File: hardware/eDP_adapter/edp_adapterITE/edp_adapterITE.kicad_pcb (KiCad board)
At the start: 4 copper layers, 36.3 x 28.4 mm, 78 parts, among them J1 DF12NB(3.0)-30DS-0.5V(51), J2 DF12NB(3.0)-30DS-0.5V(51), J3 Conn_01x30, J4 Barrel_Jack_MountingPin, J5 Conn_01x06_Socket, U1 AMS1117-1.8, U2 TLV62569APDRL, U3 MT3608, U4 IT6251, X1 27MHz

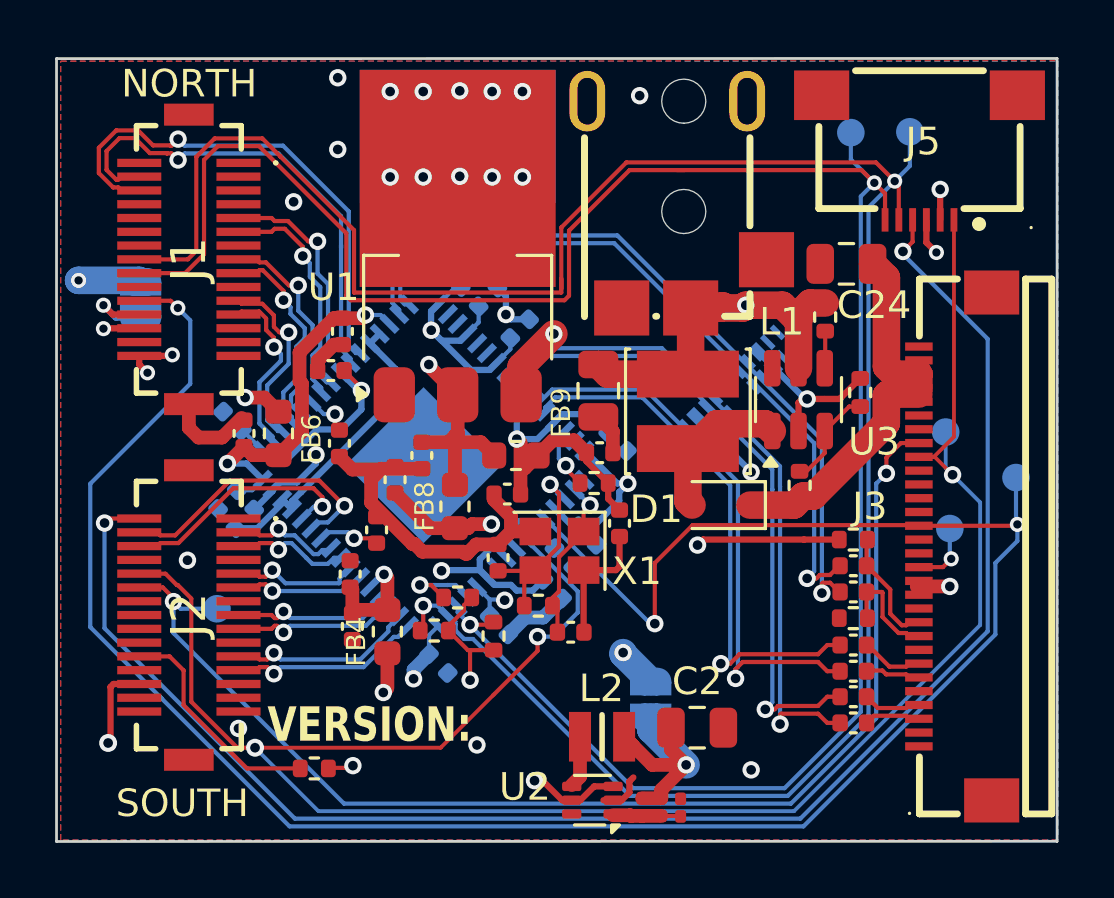
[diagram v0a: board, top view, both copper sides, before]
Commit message: add output serpentines to eDP adapter "B" board
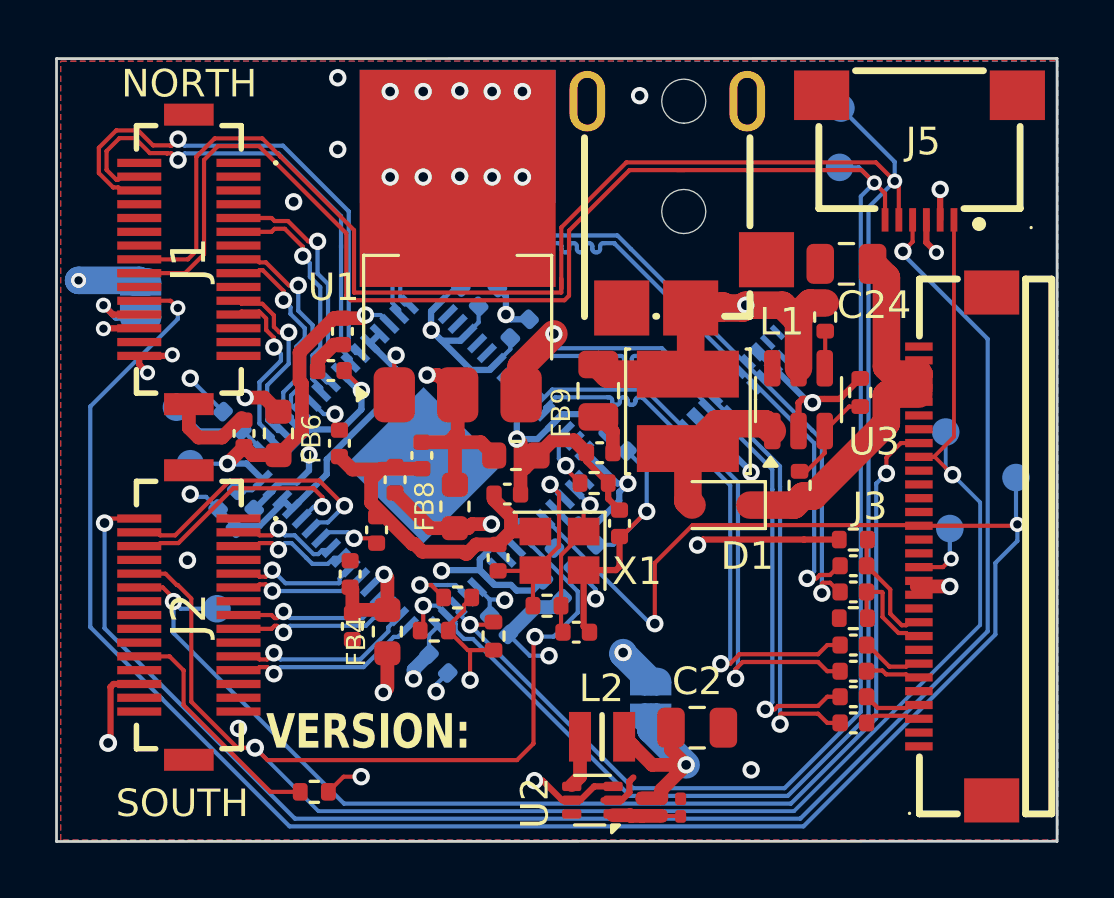
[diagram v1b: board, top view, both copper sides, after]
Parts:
- removed R18: 1M, Resistor_SMD:R_0402_1005Metric
- added R3: 1M, Resistor_SMD:R_0402_1005Metric, F.Cu at (121.4, 132.8)
- added TP2: TestPoint_Small, TestPoint:TestPoint_Pad_D1.0mm, B.Cu at (108.0, 125.5)
- added TP3: TestPoint_Small, TestPoint:TestPoint_Pad_D1.0mm, B.Cu at (108.5, 127.6)
- moved TP13 2.64 mm to (132.1, 114.7)
- moved TP14 1.33 mm to (132.0, 116.8)
- moved R9 0.85 mm to (113.0, 139.5)
- moved C19 0.20 mm to (122.5, 133.7)
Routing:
- net GND: track 57.7 -> 73.9 mm, vias 13 -> 19
- net +1V8: track 43.6 -> 46.3 mm
- net ANVDD_1V8: track 58.2 -> 60.9 mm
- net +3V3: track 107.4 -> 110.0 mm
- net PSEL: track 74.5 -> 76.8 mm
- net SDA: track 83.3 -> 84.7 mm
- net IVDD_1V8: track 30.9 -> 32.2 mm
- net /DPAUX_P: track 26.0 -> 27.3 mm
- net /DPO1_P: track 23.2 -> 24.0 mm
- net AVCC_3V3: track 49.2 -> 49.9 mm
- net SCK: track 80.6 -> 79.9 mm
- net /DPO0_P: track 19.7 -> 20.4 mm
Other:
- board text added: "eDP Adapter {dblquote}B{dblquote} v0.09"
- board text removed: "eDP Adapter IT v0.09"

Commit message: change 6-pin I2C connector to one with top contacts
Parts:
- J5: footprint easyeda2kicad:FPC-SMD_FH52K-6S-0.5SH -> easyeda2kicad:CONN-SMD_527450697; moved to B.Cu
- moved TP14 3.49 mm to (129.1, 118.8)
- moved J3 3.35 mm to (136.2, 127.2)
- moved C2 3.00 mm to (124.4, 135.5), turned to 90 degrees
- moved L2 2.46 mm to (121.5, 136.0)
- moved U2 2.46 mm to (121.1, 138.3)
- moved R11 2.46 mm to (123.6, 138.5)
- moved R12 2.46 mm to (124.3, 138.6)
- moved C6 2.46 mm to (122.9, 138.5)
- moved TP7 2.14 mm to (135.4, 127.9)
- moved J5 1.64 mm to (134.3, 118.0), turned to -90 degrees
- moved R9 1.21 mm to (113.1, 138.3)
- moved TP13 0.93 mm to (131.2, 114.9)
- moved TP5 0.79 mm to (135.4, 125.8)
- moved JP2 0.70 mm to (125.4, 135.5)
- moved R19 0.68 mm to (130.9, 127.8), turned to 180 degrees
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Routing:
- net /IO/TP_INT: track 59.2 -> 68.1 mm, vias 2 -> 1
- net GND: track 73.9 -> 82.7 mm, vias 19 -> 28
- net /IO/LCD_PWM: track 44.7 -> 49.7 mm
- net +3V3_DISP: track 24.7 -> 28.2 mm
- net TX1_N: track 2.05 -> 4.46 mm
- net SDA: track 84.7 -> 82.3 mm
- net +3V3: track 110.0 -> 107.8 mm
- net TX0_N: track 1.98 -> 4.14 mm
- net TX1_P: track 2.11 -> 4.19 mm
- net HPD: track 80.7 -> 82.8 mm
- net PSEL: track 76.8 -> 78.5 mm
- net TX0_P: track 2.26 -> 3.63 mm
- net SCK: track 79.9 -> 78.7 mm
- net BACKLIGHT_POWER: track 14.1 -> 15.3 mm
- net /IO/LCD_TEST: track 2.42 -> 3.61 mm
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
